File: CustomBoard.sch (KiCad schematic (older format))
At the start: 25 parts, among them J1 RIGHT, J10 Sensor08, J11 Sensor09, J12 Sensor10, J13 Sensor11, J14 Sensor12, J15 Sensor13, J16 Sensor14, J2 LEFT, J3 Sensor01, J4 Sensor02, J5 Sensor03, J6 Sensor04, J7 Sensor05, J8 Sensor06, J9 Sensor07, U1 DS28E05, U2 PCA9555, U3 VL53L1X

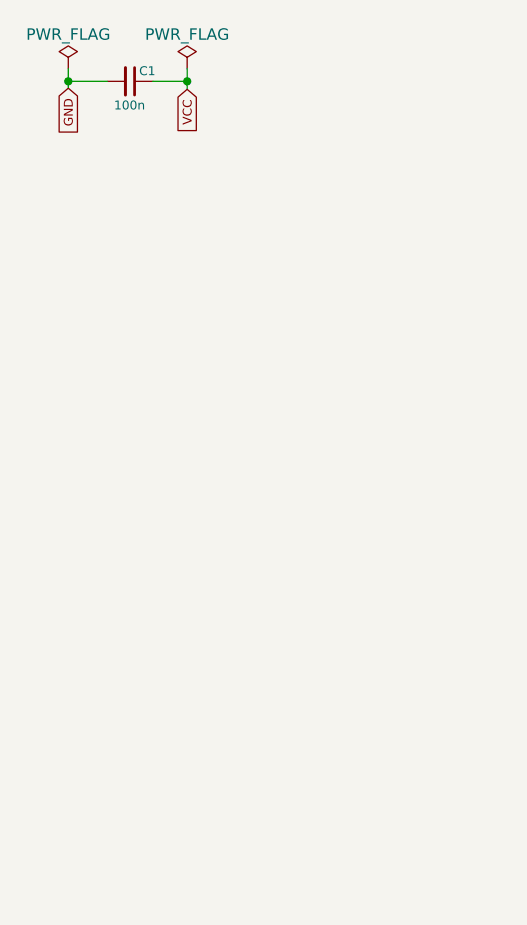
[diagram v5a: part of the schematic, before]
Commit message: pull ups
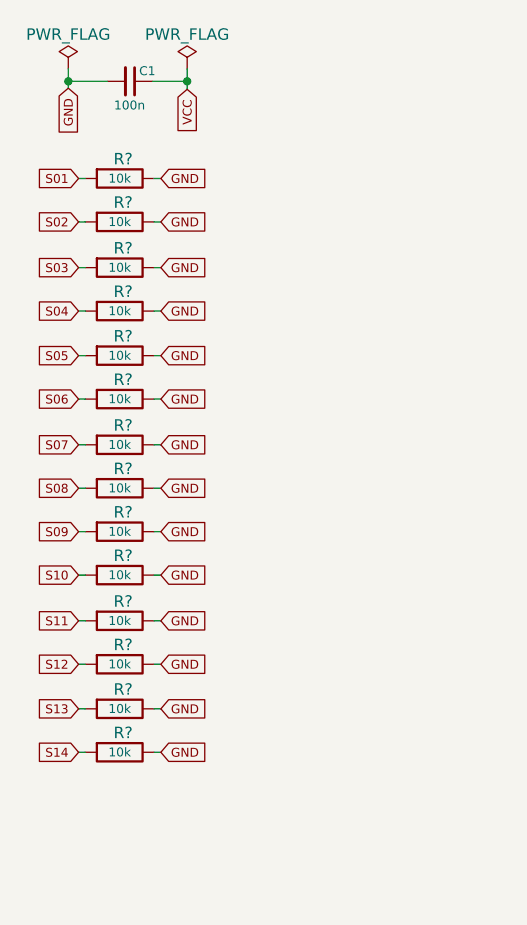
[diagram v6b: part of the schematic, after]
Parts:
- added R? (x14): 10k, symbol R
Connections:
- net GND: now also R?.1, R?.1, R?.1, R?.1, R?.1, R?.1, R?.1, R?.1, R?.1, R?.1, R?.1, R?.1, R?.1, R?.1
- net S01: now also R?.2
- net S02: now also R?.2
- net S03: now also R?.2
- net S04: now also R?.2
- net S05: now also R?.2
- net S06: now also R?.2
- net S07: now also R?.2
- net S08: now also R?.2
- net S09: now also R?.2
- net S10: now also R?.2
- net S11: now also R?.2
- net S12: now also R?.2
- net S13: now also R?.2
- net S14: now also R?.2
